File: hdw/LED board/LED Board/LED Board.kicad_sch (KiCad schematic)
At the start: 0 parts

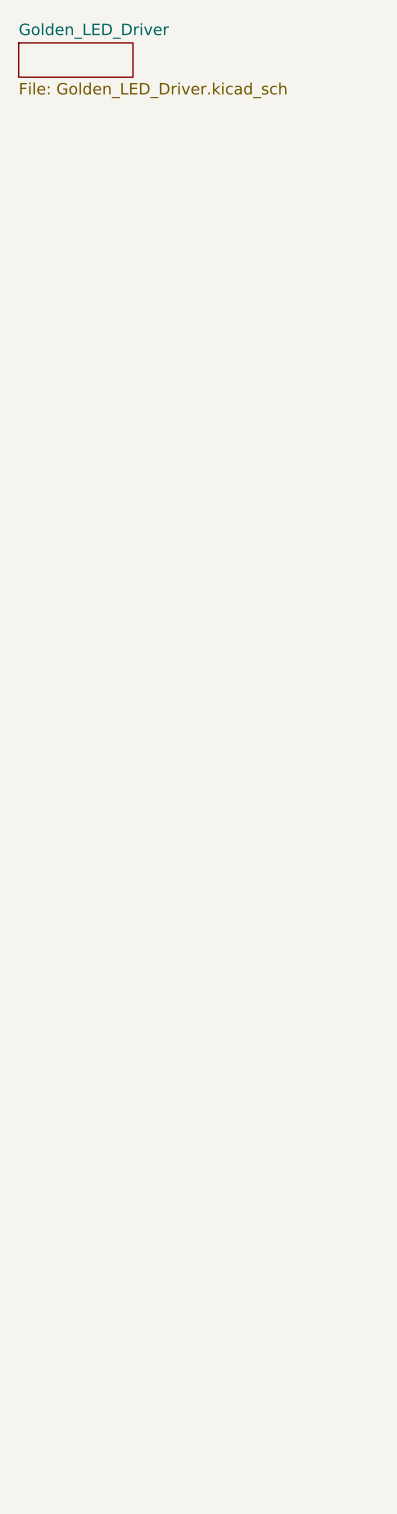
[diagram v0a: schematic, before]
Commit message: duped schematic pages and more
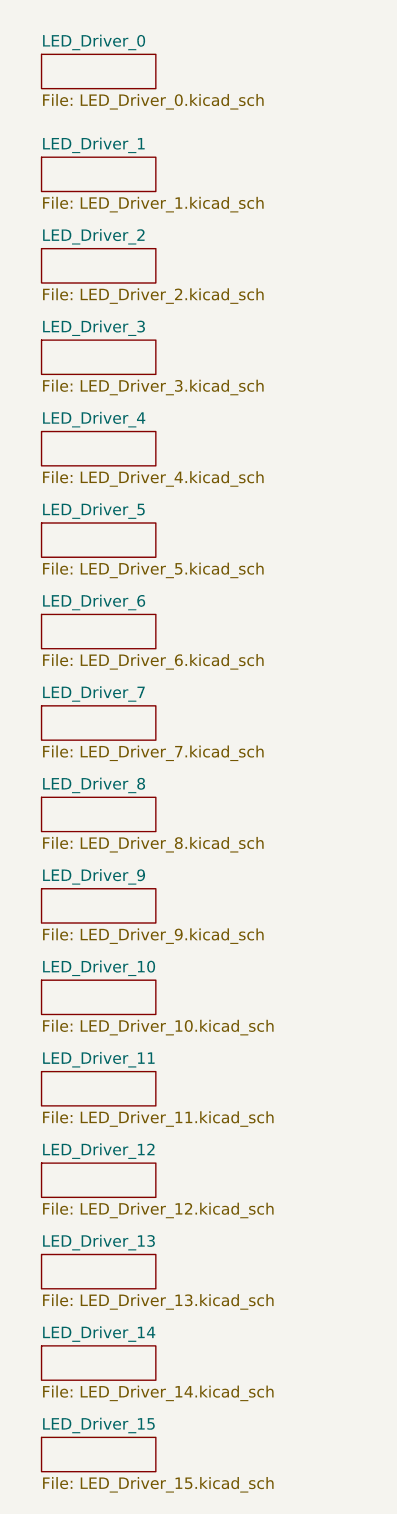
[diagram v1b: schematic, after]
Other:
- removed sheet Golden_LED_Driver
- added sheet LED_Driver_0 (LED_Driver_0.kicad_sch)
- added sheet LED_Driver_1 (LED_Driver_1.kicad_sch)
- added sheet LED_Driver_10 (LED_Driver_10.kicad_sch)
- added sheet LED_Driver_11 (LED_Driver_11.kicad_sch)
- added sheet LED_Driver_12 (LED_Driver_12.kicad_sch)
- added sheet LED_Driver_13 (LED_Driver_13.kicad_sch)
- added sheet LED_Driver_14 (LED_Driver_14.kicad_sch)
- added sheet LED_Driver_15 (LED_Driver_15.kicad_sch)
- added sheet LED_Driver_2 (LED_Driver_2.kicad_sch)
- added sheet LED_Driver_3 (LED_Driver_3.kicad_sch)
- added sheet LED_Driver_4 (LED_Driver_4.kicad_sch)
- added sheet LED_Driver_5 (LED_Driver_5.kicad_sch)
- added sheet LED_Driver_6 (LED_Driver_6.kicad_sch)
- added sheet LED_Driver_7 (LED_Driver_7.kicad_sch)
- added sheet LED_Driver_8 (LED_Driver_8.kicad_sch)
- added sheet LED_Driver_9 (LED_Driver_9.kicad_sch)

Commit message: started LED power supply
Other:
- added sheet LED_Power (LED_Power.kicad_sch)
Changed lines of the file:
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@@
+	)
+	(sheet
+		(at 139.7 35.56)
+		(size 12.7 3.81)
+		(exclude_from_sim no)
+		(in_bom yes)
+		(on_board yes)
+		(dnp no)
+		(fields_autoplaced yes)
+		(stroke
+			(width 0.1524)
+			(type solid)
+		)
+		(fill
+			(color 0 0 0 0)
+		)
+		(property "Sheetname" "LED_Power"
+			(at 139.7 34.8484 0)
+			(show_name no)
+			(do_not_autoplace no)
+			(effects
+				(font
+					(size 1.27 1.27)
+				)
+				(justify left bottom)
+			)
+		)
+		(property "Sheetfile" "LED_Power.kicad_sch"
+			(at 139.7 39.9546 0)
+			(show_name no)
+			(do_not_autoplace no)
+			(effects
+				(font
+					(size 1.27 1.27)
+				)
+				(justify left top)
+			)
+		)
+		(instances
+			(project "LED Board"
+				(path "/073a84d5-f963-4c01-a807-6da62fd6dc7d"
+					(page "2")
+				)
+			)
+		)
 	)
 	(sheet

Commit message: finished LED Power supply. Created page for 3P3 Supply
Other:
- added sheet POS3P3_Supply (POS3P3_Supply.kicad_sch)
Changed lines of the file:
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@@
+	)
+	(sheet
+		(at 139.7 45.72)
+		(size 12.7 3.81)
+		(exclude_from_sim no)
+		(in_bom yes)
+		(on_board yes)
+		(dnp no)
+		(fields_autoplaced yes)
+		(stroke
+			(width 0.1524)
+			(type solid)
+		)
+		(fill
+			(color 0 0 0 0)
+		)
+		(property "Sheetname" "POS3P3_Supply"
+			(at 139.7 45.0084 0)
+			(show_name no)
+			(do_not_autoplace no)
+			(effects
+				(font
+					(size 1.27 1.27)
+				)
+				(justify left bottom)
+			)
+		)
+		(property "Sheetfile" "POS3P3_Supply.kicad_sch"
+			(at 139.7 50.1146 0)
+			(show_name no)
+			(do_not_autoplace no)
+			(effects
+				(font
+					(size 1.27 1.27)
+				)
+				(justify left top)
+			)
+		)
+		(instances
+			(project "LED Board"
+				(path "/073a84d5-f963-4c01-a807-6da62fd6dc7d"
+					(page "19")
+				)
+			)
+		)
 	)
 	(sheet

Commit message: added connectors, updated some signal names on labels
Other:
- added sheet led_panel_connector (led_panel_connector.kicad_sch)
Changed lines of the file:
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@@
+	)
+	(sheet
+		(at 139.7 57.15)
+		(size 12.7 3.81)
+		(exclude_from_sim no)
+		(in_bom yes)
+		(on_board yes)
+		(dnp no)
+		(fields_autoplaced yes)
+		(stroke
+			(width 0.1524)
+			(type solid)
+		)
+		(fill
+			(color 0 0 0 0)
+		)
+		(property "Sheetname" "led_panel_connector"
+			(at 139.7 56.4384 0)
+			(show_name no)
+			(do_not_autoplace no)
+			(effects
+				(font
+					(size 1.27 1.27)
+				)
+				(justify left bottom)
+			)
+		)
+		(property "Sheetfile" "led_panel_connector.kicad_sch"
+			(at 139.7 61.5446 0)
+			(show_name no)
+			(do_not_autoplace no)
+			(effects
+				(font
+					(size 1.27 1.27)
+				)
+				(justify left top)
+			)
+		)
+		(instances
+			(project "LED Board"
+				(path "/073a84d5-f963-4c01-a807-6da62fd6dc7d"
+					(page "20")
+				)
+			)
+		)
 	)
 	(sheet
